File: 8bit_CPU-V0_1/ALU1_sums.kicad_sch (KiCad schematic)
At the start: 4 parts, among them U14 74LS283, U15 74LS283

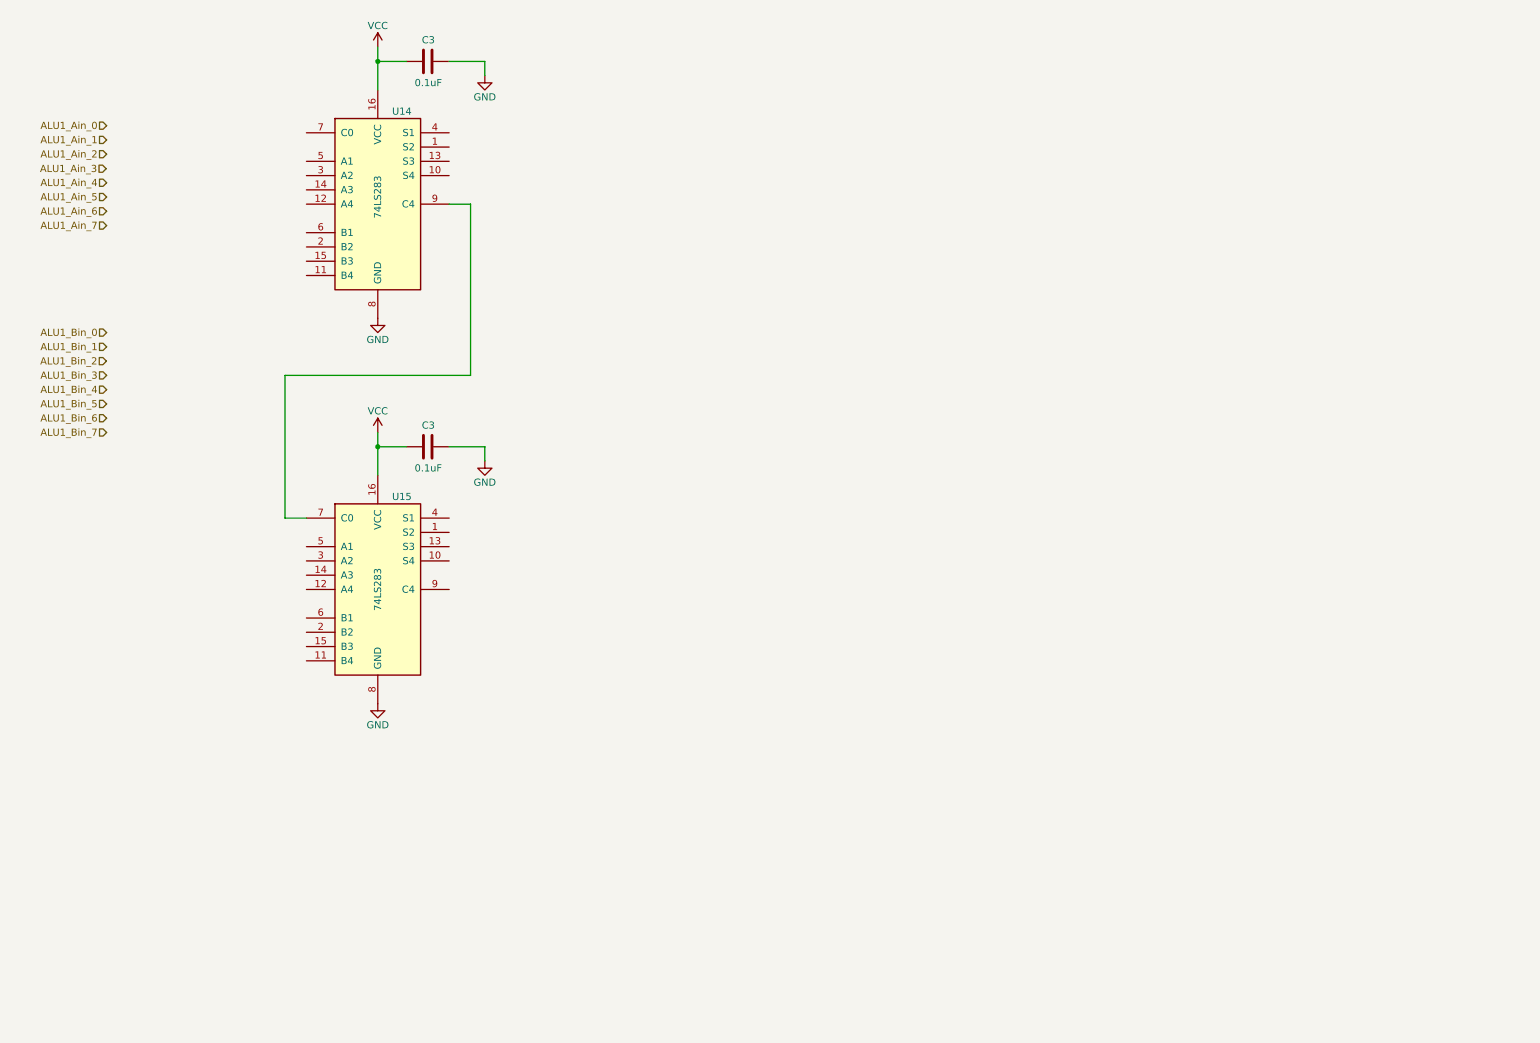
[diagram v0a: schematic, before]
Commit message: Modifications
-Nammed sub parts of circuits
-Created new prepared sheets for ALU ANDS and EORS
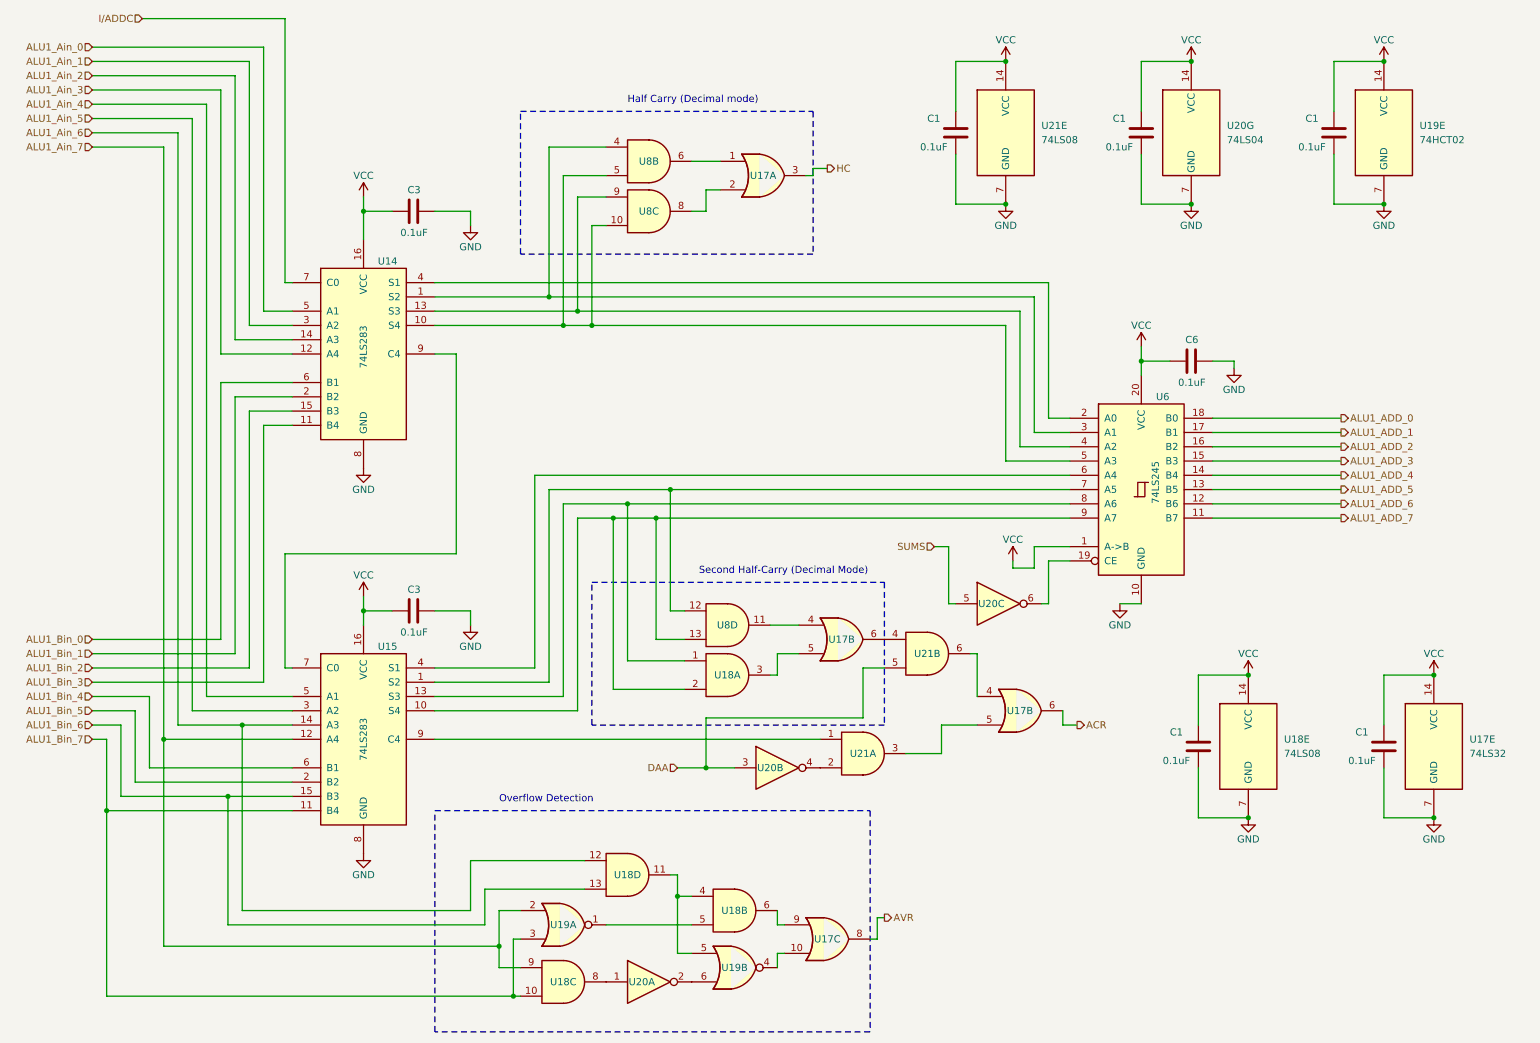
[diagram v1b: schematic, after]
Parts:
- added C1 (x5), C6: 0.1uF, symbol Device:C
- added U17 (x2): 74LS32, symbol 74xx:74LS32
- added U18, U21, U8: 74LS08, symbol 74xx:74LS08
- added U19: 74HCT02, symbol 74xx:74HCT02
- added U20: 74LS04, symbol 74xx:74LS04
- added U6: 74LS245, symbol 74xx:74LS245
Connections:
- net ALU1_Ain_0: now also U14.5 (A1)
- net ALU1_Ain_1: now also U14.3 (A2)
- net ALU1_Ain_2: now also U14.14 (A3)
- net ALU1_Ain_3: now also U14.12 (A4)
- net ALU1_Ain_4: now also U15.5 (A1)
- net ALU1_Ain_5: now also U15.3 (A2)
- net ALU1_Ain_6: now also U15.14 (A3), U18.12
- net ALU1_Ain_7: now also U15.12 (A4), U18.9, U19.2
- net ALU1_Bin_0: now also U14.6 (B1)
- net ALU1_Bin_1: now also U14.2 (B2)
- net ALU1_Bin_2: now also U14.15 (B3)
- net ALU1_Bin_3: now also U14.11 (B4)
- net ALU1_Bin_4: now also U15.6 (B1)
- net ALU1_Bin_5: now also U15.2 (B2)
- net ALU1_Bin_6: now also U15.15 (B3), U18.13
- net ALU1_Bin_7: now also U15.11 (B4), U18.10, U19.3
- net GND: now also C1.2, C1.2, C1.2, C1.2, C1.2, C6.2, U17.7 (GND), U18.7 (GND), U19.7 (GND), U20.7 (GND), U21.7 (GND), U6.10 (GND)
- net VCC: now also C1.1, C1.1, C1.1, C1.1, C1.1, C6.1, U17.14 (VCC), U18.14 (VCC), U19.14 (VCC), U20.14 (VCC), U21.14 (VCC), U6.1 (A->B), U6.20 (VCC)
- net at U15.1 (S2): now also U6.7 (A5), U8.12
- net at U15.10 (S4): now also U18.2, U6.9 (A7), U8.13
- net at U15.13 (S3): now also U18.1, U6.8 (A6)
- net at U15.4 (S1): now also U6.6 (A4)
- net at U15.9 (C4): now also U21.1
- net at U14.1 (S2): now also U6.3 (A1), U8.4
- net at U14.10 (S4): now also U6.5 (A3), U8.10, U8.5
- net at U14.13 (S3): now also U6.4 (A2), U8.9
- net at U14.4 (S1): now also U6.2 (A0)
- net I/ADDC: now reaches U14.7 (C0)
- new net: U17.2, U8.8
- new net: U17.4, U8.11
- new net: U17.5, U18.3
- new net: U17.6, U21.4
- new net: U17.4, U21.6
- new net: U20.4, U21.2
- new net: U17.1, U8.6
- new net: U18.8, U20.1
- new net: U18.11, U18.4, U19.5
- new net: U20.6, U6.19 (CE)
- new net: U17.5, U21.3
- new net: U17.10, U19.4
- new net: U17.9, U18.6
- new net: U19.6, U20.2
- new net: U18.5, U19.1
- new net ACR: U17.6
- new net ALU1_ADD_0: U6.18 (B0)
- new net ALU1_ADD_1: U6.17 (B1)
- new net ALU1_ADD_2: U6.16 (B2)
- new net ALU1_ADD_3: U6.15 (B3)
- new net ALU1_ADD_4: U6.14 (B4)
- new net ALU1_ADD_5: U6.13 (B5)
- new net ALU1_ADD_6: U6.12 (B6)
- new net ALU1_ADD_7: U6.11 (B7)
- new net AVR: U17.8
- new net DAA: U20.3, U21.5
- new net HC: U17.3
- new net SUMS: U20.5
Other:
- note added: "Half Carry (Decimal mode)"
- note added: "Overflow Detection"
- note added: "Second Half-Carry (Decimal Mode)"
- moved on the sheet: C3, U14, U15

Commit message: ALU finished
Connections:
- net ACR renamed SUMS_CARRY(ALU5)
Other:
- company: (none) -> PRP-DIY
- title: (none) -> PRP-6502 -- ALU1 : SUMS
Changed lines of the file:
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@@
 (kicad_sch (version 20230121) (generator eeschema)
   (paper "A4")
+  (title_block
+    (title "PRP-6502 -- ALU1 : SUMS")
+    (date "2023-07-02")
+    (company "PRP-DIY")
+  )
   (junction (at 234.95 132.08) (diameter 0) (color 0 0 0 0)
   )
@@
     (stroke (width 0) (type default))
   )
+  (wire (pts (xy 210.82 138.43) (xy 201.93 138.43))
+    (stroke (width 0) (type default))
+  )
   (wire (pts (xy 182.88 39.37) (xy 182.88 48.26))
     (stroke (width 0) (type default))
@@
     (stroke (width 0) (type default))
   )
-  (wire (pts (xy 201.93 138.43) (xy 201.93 140.97))
+  (wire (pts (xy 210.82 154.94) (xy 210.82 138.43))
     (stroke (width 0) (type default))
   )
@@
     (stroke (width 0) (type default))
   )
-  (wire (pts (xy 201.93 140.97) (xy 204.47 140.97))
+  (wire (pts (xy 210.82 154.94) (xy 198.12 154.94))
     (stroke (width 0) (type default))
   )
@@
     (effects (font (size 1.27 1.27)) (justify right))
   )
-  (hierarchical_label "ACR" (shape output) (at 204.47 140.97 0) (fields_autoplaced)
-    (effects (font (size 1.27 1.27)) (justify left))
+  (hierarchical_label "SUMS_CARRY(ALU5)" (shape output) (at 198.12 154.94 180) (fields_autoplaced)
+    (effects (font (size 1.27 1.27)) (justify right))
   )
   (hierarchical_label "ALU1_Ain_7" (shape input) (at 29.21 38.1 180) (fields_autoplaced)
@@
         )
         (path "/81b49a11-4d6c-4532-89fe-728a8cf00278/2506dba5-d3a6-49a3-9eb6-4c25813b2799"
-          (reference "C21") (unit 1)
+          (reference "C17") (unit 1)
         )
       )
@@
         )
         (path "/81b49a11-4d6c-4532-89fe-728a8cf00278/2506dba5-d3a6-49a3-9eb6-4c25813b2799"
-          (reference "C18") (unit 1)
+          (reference "C20") (unit 1)
         )
       )
@@
         )
         (path "/81b49a11-4d6c-4532-89fe-728a8cf00278/2506dba5-d3a6-49a3-9eb6-4c25813b2799"
-          (reference "C20") (unit 1)
+          (reference "C18") (unit 1)
         )
       )
@@
         )
         (path "/81b49a11-4d6c-4532-89fe-728a8cf00278/2506dba5-d3a6-49a3-9eb6-4c25813b2799"
-          (reference "C17") (unit 1)
-        )
-      )
+          (reference "C21") (unit 1)
+        )
+      )

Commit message: Refining schematics
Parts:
- added D5 (x2): LED, symbol Device:LED
- added R1 (x2): 330, symbol Device:R_US
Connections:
- net AVR: now also D5.2 (A)
- net GND: now also R1.2, R1.2
- net HC: now also D5.2 (A)
- new net: D5.1 (K), R1.1 (x2)
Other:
- moved on the sheet: C1, U17A, U17E, U18E, U8B, U8C

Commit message: New update
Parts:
- removed C1: 0.1uF, symbol Device:C
- removed D5 (x2): LED, symbol Device:LED
- removed R1 (x2): 330, symbol Device:R_US
- removed unit 3 of U17
- removed unit 3 of U18
- removed unit 4 of U18
- removed unit 2 of U18
- removed U19: 74HCT02, symbol 74xx:74HCT02
- removed unit 2 of U20
- removed unit 1 of U20
- added D5: LED, symbol Device:LED
- added R1: 330, symbol Device:R_US
- added unit 3 of U26
- added unit 4 of U30
- added unit 3 of U31
- added unit 4 of U31
- renumbered U15 to U13, U20 to U26, U17 to U30, U21 to U31, U18 to U31, U8 to U32, U18 to U32, U21 to U32
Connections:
- net DAA: now also U31.2, U26.5, U31.13; no longer U31.5
- net GND: now also R1.1
- net HC: now also D5.2 (A), U30.11; no longer U30.3
- net SUMS: now also U26.9; no longer U26.5
- net SUMS_CARRY(ALU5): now also U30.3; no longer U30.6
- net at U14.10 (S4), U32.10, U6.5 (A3): now also U32.13; no longer U32.5
- net at U32.8: now also U30.10; no longer U30.2
- net at U30.4: now also U32.6; no longer U32.11
- net at U30.6: now also U31.1; no longer U31.4
- net AVR_SUMS_OUT: now reaches U13.10 (S4), U32.2, U6.9 (A7)
- net AVR_SUMS_OUT: now also U32.5; no longer U32.13
- net at U13.1 (S2), U6.7 (A5): now also U32.4; no longer U32.12
- net at U6.19 (CE): now also U26.8; no longer U26.6
- net at U14.1 (S2), U6.3 (A1): now also U32.12; no longer U32.4
- net at U13.9 (C4): now also U31.4; no longer U31.1
- net at U13.7 (C0), U14.9 (C4): now also U31.9
- new net: D5.1 (K), R1.2
- new net: U30.1, U31.3
- new net: U30.8, U31.12
- new net: U30.9, U32.11
- new net: U26.6, U31.10, U31.5
- new net: U30.2, U31.6
- new net: U30.13, U31.8
- new net: U30.12, U31.11
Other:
- note removed: "Overflow Detection"
- moved on the sheet: C1, U26G, U30A, U30B, U31A, U31B, U32A, U32B, U32E
